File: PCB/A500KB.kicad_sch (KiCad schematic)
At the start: 251 parts, among them J1 Conn_01x31, J2 USB_B_Micro, J3 Conn_02x03_Odd_Even, J4 Conn_01x08_Male, J5 Conn_01x02, J6 Conn_01x04_Male, J7 Conn_01x04, Q1 MMBT3904, U1 IS32FL3237_DS, U2 AT90USB1287-A, Y2 16 MHz

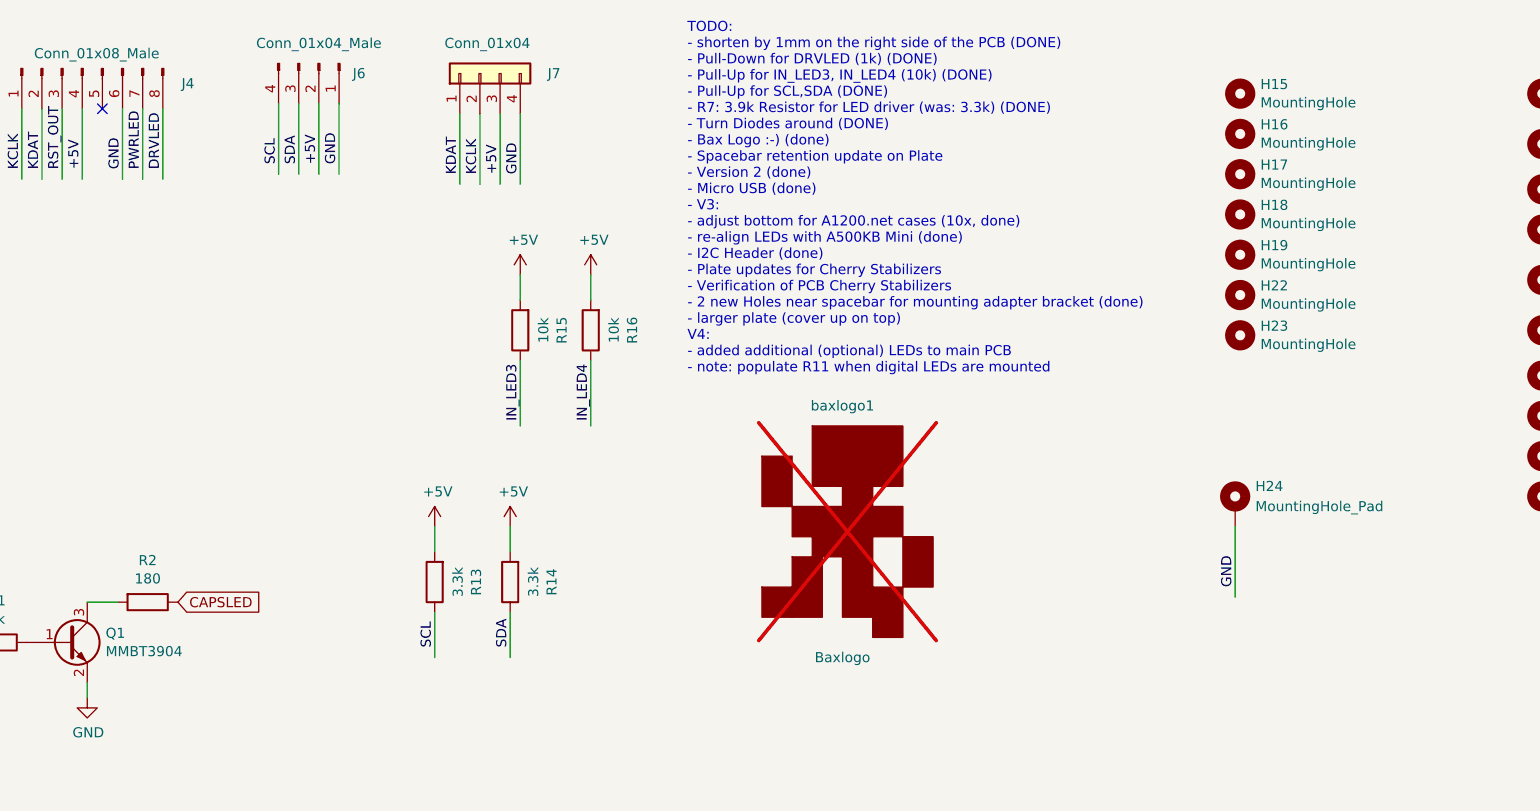
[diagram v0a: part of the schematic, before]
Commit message: V4c: fixed connector for A2k-A4k keyboard cables
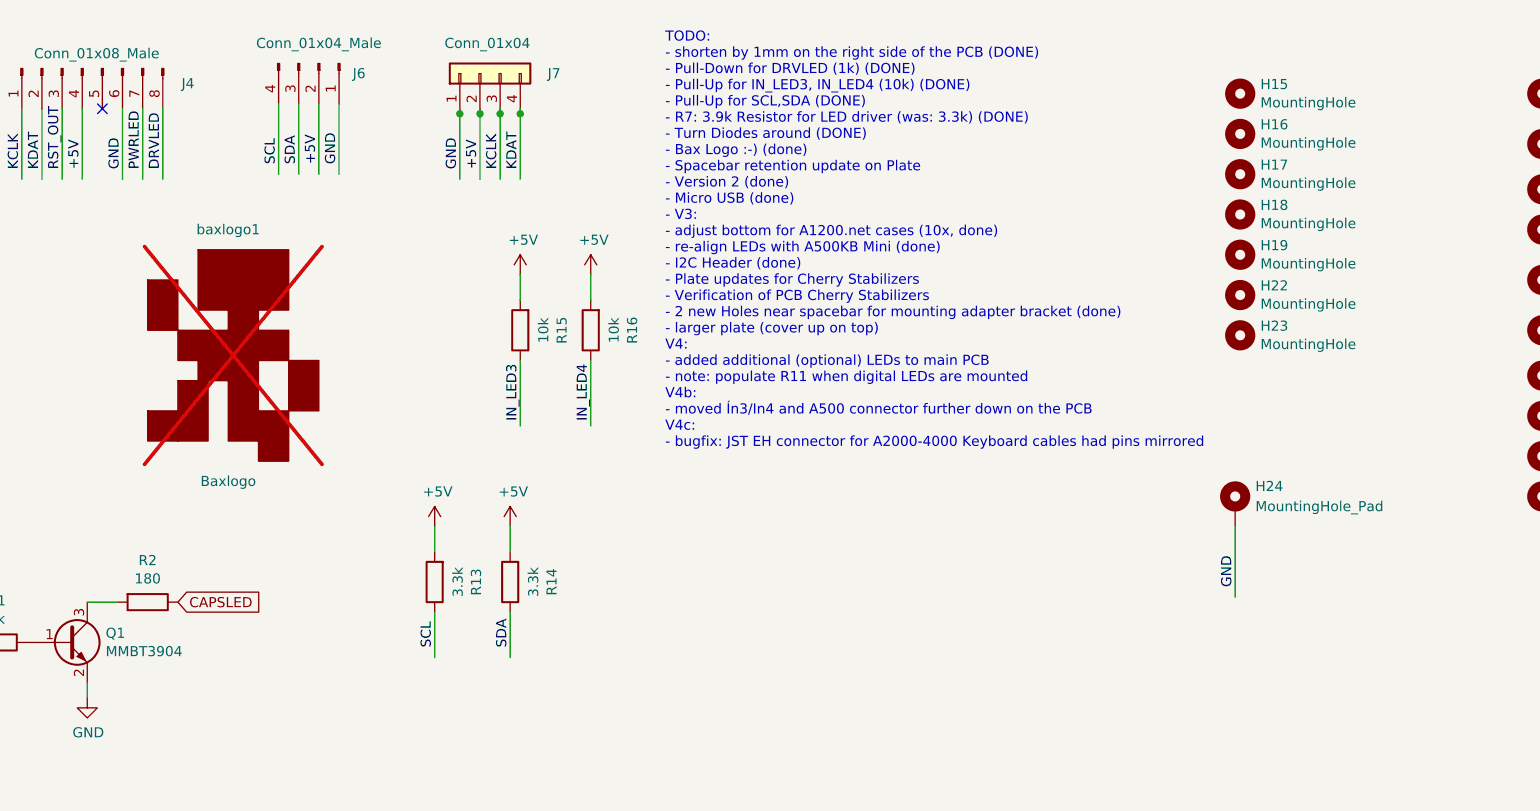
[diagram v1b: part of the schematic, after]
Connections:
- net +5V: now also J7.2 (Pin_2); no longer J7.3 (Pin_3)
- net GND: now also J7.1 (Pin_1); no longer J7.4 (Pin_4)
- net KCLK: now also J7.3 (Pin_3); no longer J7.2 (Pin_2)
- net KDAT: now also J7.4 (Pin_4); no longer J7.1 (Pin_1)
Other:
- moved on the sheet: baxlogo1
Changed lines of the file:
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@@
 	)
 	(junction
+		(at 252.73 26.035)
+		(diameter 0)
+		(color 0 0 0 0)
+	)
+	(junction
 		(at 132.08 354.33)
 		(diameter 0)
@@
 	)
 	(junction
+		(at 257.81 26.035)
+		(diameter 0)
+		(color 0 0 0 0)
+	)
+	(junction
 		(at 261.62 333.375)
 		(diameter 0)
@@
 	)
 	(junction
+		(at 250.19 26.035)
+		(diameter 0)
+		(color 0 0 0 0)
+	)
+	(junction
 		(at 257.175 234.315)
 		(diameter 0)
@@
 	)
 	(junction
+		(at 255.27 26.035)
+		(diameter 0)
+		(color 0 0 0 0)
+	)
+	(junction
 		(at 86.36 285.75)
 		(diameter 0)
@@
 	(wire
 		(pts
+			(xy 255.27 26.035) (xy 255.27 34.29)
+		)
+		(stroke
+			(width 0)
+			(type default)
+		)
+	)
+	(wire
+		(pts
 			(xy 71.12 376.555) (xy 86.36 376.555)
 		)
@@
 	(wire
 		(pts
-			(xy 257.81 26.035) (xy 257.81 34.925)
+			(xy 250.19 25.4) (xy 250.19 26.035)
 		)
 		(stroke
@@
 	(wire
 		(pts
+			(xy 257.81 26.035) (xy 257.81 34.29)
+		)
+		(stroke
+			(width 0)
+			(type default)
+		)
+	)
+	(wire
+		(pts
 			(xy 78.105 339.725) (xy 91.44 339.725)
 		)
@@
 	(wire
 		(pts
-			(xy 255.27 26.035) (xy 255.27 34.925)
+			(xy 252.73 25.4) (xy 252.73 26.035)
 		)
 		(stroke
@@
 	(wire
 		(pts
-			(xy 250.19 26.035) (xy 250.19 34.925)
+			(xy 257.81 25.4) (xy 257.81 26.035)
 		)
 		(stroke
@@
 	(wire
 		(pts
-			(xy 252.73 26.035) (xy 252.73 34.925)
+			(xy 255.27 25.4) (xy 255.27 26.035)
 		)
 		(stroke
@@
 	(wire
 		(pts
+			(xy 250.19 26.035) (xy 250.19 34.29)
+		)
+		(stroke
+			(width 0)
+			(type default)
+		)
+	)
+	(wire
+		(pts
 			(xy 170.815 297.18) (xy 170.815 300.99)
 		)
@@
 	(wire
 		(pts
+			(xy 252.73 26.035) (xy 252.73 34.29)
+		)
+		(stroke
+			(width 0)
+			(type default)
+		)
+	)
+	(wire
+		(pts
 			(xy 199.39 295.275) (xy 199.39 316.23)
 		)
@@
 		)
 	)
-	(text "TODO:\n- shorten by 1mm on the right side of the PCB (DONE)\n- Pull-Down for DRVLED (1k) (DONE)\n- Pull-Up for IN_LED3, IN_LED4 (10k) (DONE)\n- Pull-Up for SCL,SDA (DONE)\n- R7: 3.9k Resistor for LED driver (was: 3.3k) (DONE)\n- Turn Diodes around (DONE)\n- Bax Logo :-) (done)\n- Spacebar retention update on Plate\n- Version 2 (done)\n- Micro USB (done)\n- V3:\n- adjust bottom for A1200.net cases (10x, done)\n- re-align LEDs with A500KB Mini (done)\n- I2C Header (done)\n- Plate updates for Cherry Stabilizers\n- Verification of PCB Cherry Stabilizers\n- 2 new Holes near spacebar for mounting adapter bracket (done)\n- larger plate (cover up on top)\nV4:\n- added additional (optional) LEDs to main PCB\n- note: populate R11 when digital LEDs are mounted"
+	(text "TODO:\n- shorten by 1mm on the right side of the PCB (DONE)\n- Pull-Down for DRVLED (1k) (DONE)\n- Pull-Up for IN_LED3, IN_LED4 (10k) (DONE)\n- Pull-Up for SCL,SDA (DONE)\n- R7: 3.9k Resistor for LED driver (was: 3.3k) (DONE)\n- Turn Diodes around (DONE)\n- Bax Logo :-) (done)\n- Spacebar retention update on Plate\n- Version 2 (done)\n- Micro USB (done)\n- V3:\n- adjust bottom for A1200.net cases (10x, done)\n- re-align LEDs with A500KB Mini (done)\n- I2C Header (done)\n- Plate updates for Cherry Stabilizers\n- Verification of PCB Cherry Stabilizers\n- 2 new Holes near spacebar for mounting adapter bracket (done)\n- larger plate (cover up on top)\nV4:\n- added additional (optional) LEDs to main PCB\n- note: populate R11 when digital LEDs are mounted\nV4b:\n- moved Ín3/In4 and A500 connector further down on the PCB\nV4c:\n- bugfix: JST EH connector for A2000-4000 Keyboard cables had pins mirrored"
 		(exclude_from_sim no)
-		(at 278.892 58.928 0)
+		(at 276.098 68.326 0)
 		(effects
 			(font
@@
 	)
 	(label "KCLK"
-		(at 252.73 33.655 90)
+		(at 255.27 33.02 90)
 		(fields_autoplaced yes)
 		(effects
@@
 	)
 	(label "KDAT"
-		(at 250.19 33.655 90)
+		(at 257.81 33.02 90)
 		(fields_autoplaced yes)
 		(effects
@@
 	)
 	(label "+5V"
-		(at 255.27 33.655 90)
+		(at 252.73 33.02 90)
 		(fields_autoplaced yes)
 		(effects
@@
 	)
 	(label "GND"
-		(at 257.81 33.655 90)
+		(at 250.19 33.02 90)
 		(fields_autoplaced yes)
 		(effects
@@
 	(symbol
 		(lib_id "Graphic:Logo_Open_Hardware_Small")
-		(at 298.45 78.105 0)
+		(at 220.98 55.88 0)
 		(unit 1)
 		(exclude_from_sim no)
@@
 		(dnp yes)
 		(property "Reference" "baxlogo1"
-			(at 298.45 62.865 0)
+			(at 220.98 40.64 0)
 			(effects
 				(font
@@
 		)
 		(property "Value" "Baxlogo"
-			(at 298.45 94.615 0)
+			(at 220.98 72.39 0)
 			(effects
 				(font
@@
 		)
 		(property "Footprint" "Bax:baxlogo"
-			(at 299.72 76.835 0)
+			(at 222.25 54.61 0)
 			(effects
 				(font
@@
 		)
 		(property "Datasheet" "~"
-			(at 299.72 76.835 0)
+			(at 222.25 54.61 0)
 			(effects
 				(font
@@
 		)
 		(property "Description" ""
-			(at 298.45 78.105 0)
+			(at 220.98 55.88 0)
 			(effects
 				(font

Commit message: Hardware finetuning, Amiga program update
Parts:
- added R17: 150k, Resistor_SMD:R_0805_2012Metric_Pad1.20x1.40mm_HandSolder, symbol Device:R
- J1: value Conn_01x31 -> N/A
- J4: footprint Connector_PinHeader_2.54mm:PinHeader_1x08_P2.54mm_Vertical -> Connector_PinHeader_2.54mm:PinHeader_1x08_P2.54mm_Horizontal
- J5: footprint Connector_PinHeader_2.54mm:PinHeader_1x02_P2.54mm_Vertical -> Connector_PinHeader_2.54mm:PinHeader_1x02_P2.54mm_Horizontal; LCSC (none) -> C2935927
- J6: value Conn_01x04_Male -> N/A; DNP (none) -> true
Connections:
- net +5V: now also J7.3 (Pin_3); no longer J7.2 (Pin_2)
- net GND: now also J7.4 (Pin_4), R17.1; no longer J7.1 (Pin_1)
- net KCLK: now also J7.2 (Pin_2); no longer J7.3 (Pin_3)
- net KDAT: now also J7.1 (Pin_1); no longer J7.4 (Pin_4)
- net RST_OUT: now also R17.2
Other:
- note added: "TODO/Revision list: - shorten by 1mm on the right side of the PCB (DONE) - Pull-Down for DRVLED (1k) (DONE) - Pull-Up for IN_LED3, IN_LED4 (10k) (DONE) - Pull-Up for SCL,SDA (DONE) - R7: 3.9k Resistor for LED driver (was: 3.3k) (DONE) - Turn Diodes around (DONE) - Bax Logo :-) (done) - Spacebar retention update on Plate Version 2 (done) - Micro USB (done) V3: - adjust bottom for A1200.net cases (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"
- note removed: "TODO: - shorten by 1mm on the right side of the PCB (DONE) - Pull-Down for DRVLED (1k) (DONE) - Pull-Up for IN_LED3, IN_LED4 (10k) (DONE) - Pull-Up for SCL,SDA (DONE) - R7: 3.9k Resistor for LED driver (was: 3.3k) (DONE) - Turn Diodes around (DONE) - Bax Logo :-) (done) - Spacebar retention update on Plate - Version 2 (done) - Micro USB (done) - V3: - adjust bottom for A1200.net cases (10x, done)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"
- moved on the sheet: H24

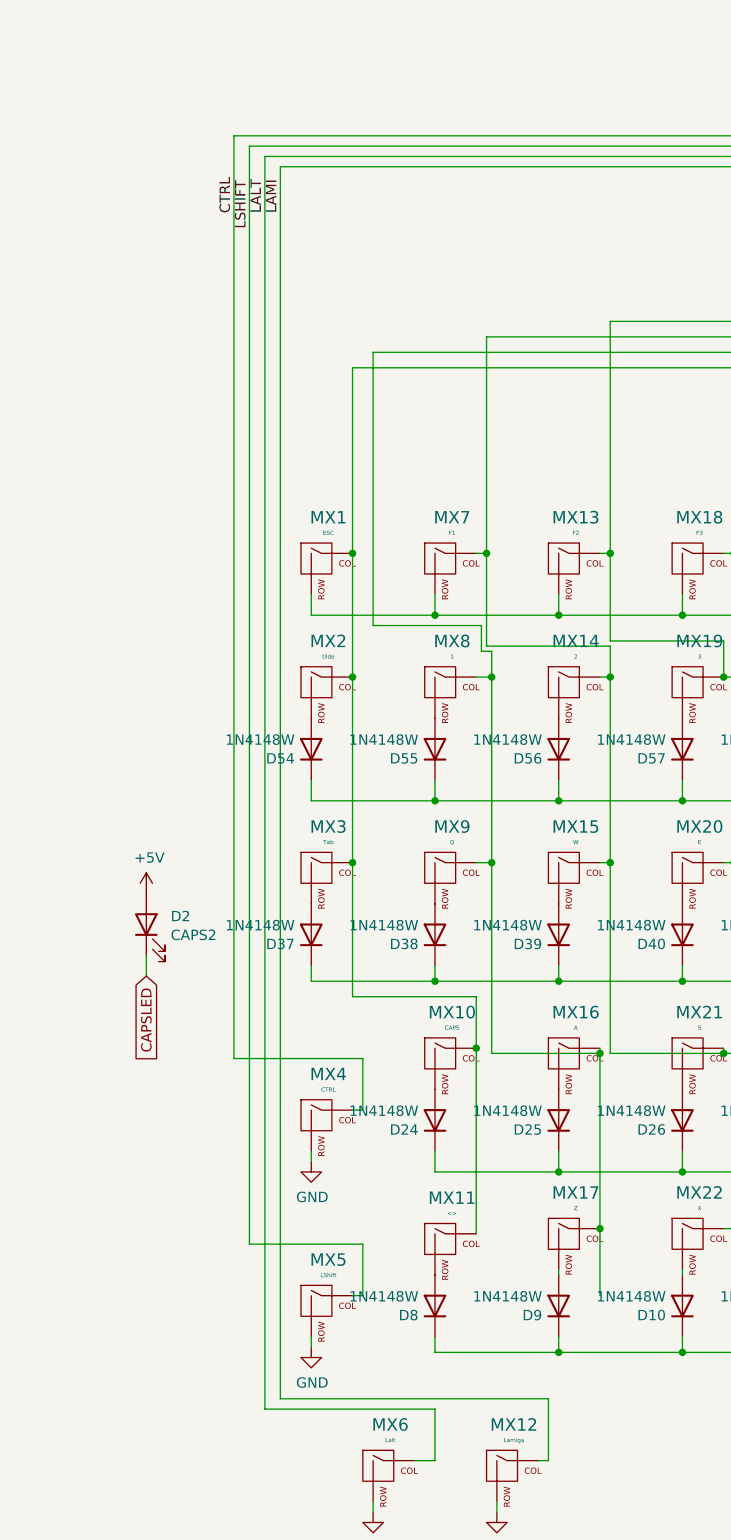
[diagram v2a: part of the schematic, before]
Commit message: unified 3D printed parts for internal/external use
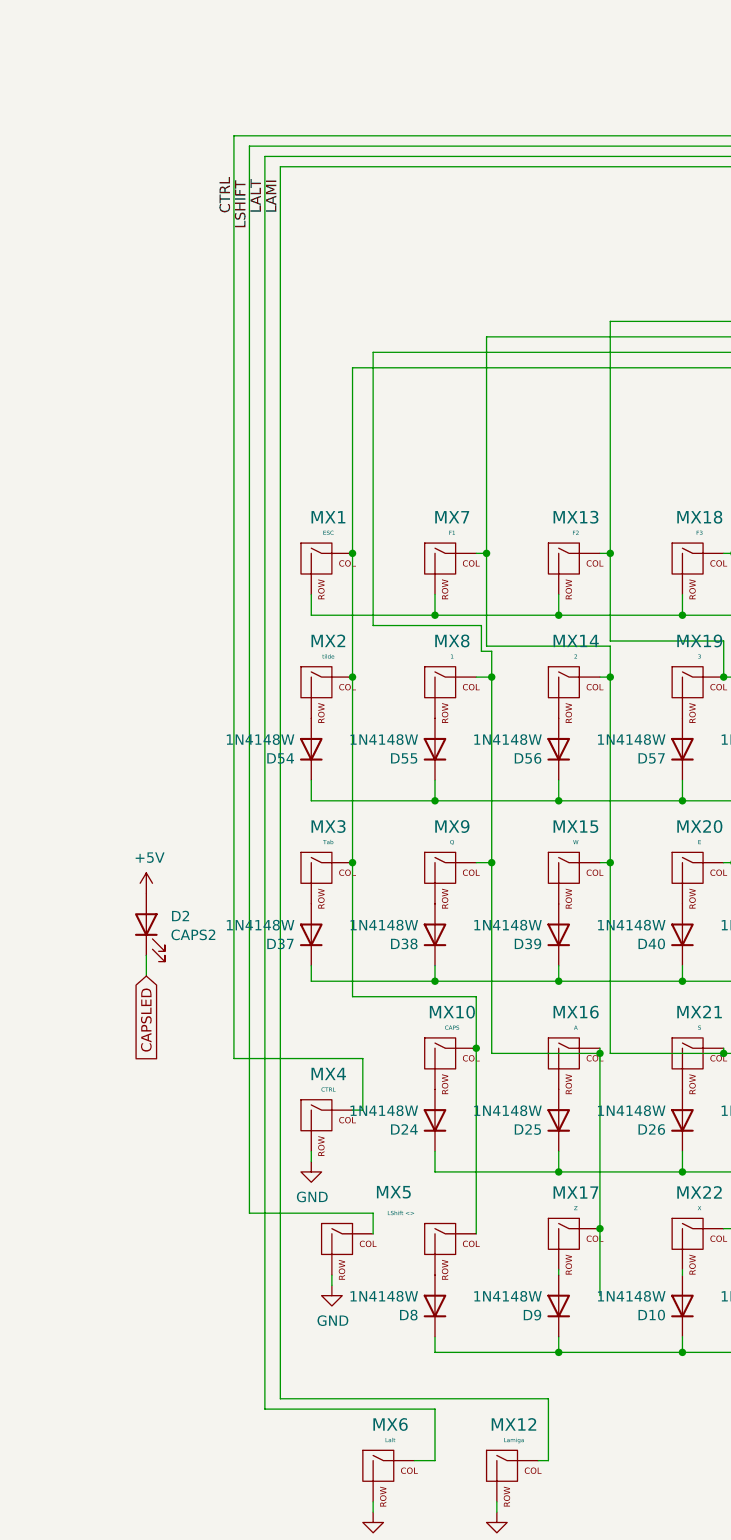
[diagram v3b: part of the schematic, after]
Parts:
- removed MX11: <>, MXMitsumi:MXMitsumi-1U-NoLED, symbol MX_Hybrid:MX-NoLED
- removed MX5: LShift, MXMitsumi:MXMitsumi-1.75U-NoLED, symbol MX_Hybrid:MX-NoLED
- added MX5: LShift <>, MXMitsumi:MXMitsumi-2.75U-SPCLEFT_LR, symbol MX_Hybrid:MX-LSHIFT_LR
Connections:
- net GND: now also MX5.2 (ROW)
- net LSHIFT: now also MX5.1 (COL)
- net Y14=15: now also MX5.3 (COL)
- net at D8.2 (A): now also MX5.4 (ROW)
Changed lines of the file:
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@@
 		(title "A500 Keyboard")
 		(date "2021-12-04")
-		(rev "0.0")
+		(rev "4e")
 		(company "Henryk Richter")
 	)
@@
 	(wire
 		(pts
+			(xy 63.5 361.95) (xy 63.5 359.41)
+		)
+		(stroke
+			(width 0)
+			(type default)
+		)
+	)
+	(wire
+		(pts
 			(xy 167.64 316.23) (xy 168.91 316.23)
 		)
@@
 	(wire
 		(pts
-			(xy 55.88 374.65) (xy 55.88 375.92)
+			(xy 58.42 367.03) (xy 58.42 368.3)
 		)
 		(stroke
@@
 	(wire
 		(pts
-			(xy 60.96 369.57) (xy 62.23 369.57)
-		)
-		(stroke
-			(width 0)
-			(type default)
-		)
-	)
-	(wire
-		(pts
 			(xy 387.35 344.17) (xy 386.08 344.17)
 		)
@@
 	(wire
 		(pts
+			(xy 48.26 359.41) (xy 48.26 227.965)
+		)
+		(stroke
+			(width 0)
+			(type default)
+		)
+	)
+	(wire
+		(pts
 			(xy 221.615 224.79) (xy 221.615 227.965)
 		)
@@
 	(wire
 		(pts
-			(xy 48.26 363.22) (xy 48.26 227.965)
-		)
-		(stroke
-			(width 0)
-			(type default)
-		)
-	)
-	(wire
-		(pts
 			(xy 515.62 86.995) (xy 526.415 86.995)
 		)
@@
 	(wire
 		(pts
-			(xy 62.23 369.57) (xy 62.23 363.22)
-		)
-		(stroke
-			(width 0)
-			(type default)
-		)
-	)
-	(wire
-		(pts
 			(xy 541.02 127) (xy 550.545 127)
 		)
@@
 	(wire
 		(pts
+			(xy 63.5 359.41) (xy 48.26 359.41)
+		)
+		(stroke
+			(width 0)
+			(type default)
+		)
+	)
+	(wire
+		(pts
 			(xy 249.555 240.03) (xy 391.16 240.03)
 		)
@@
 	(wire
 		(pts
-			(xy 62.23 363.22) (xy 48.26 363.22)
-		)
-		(stroke
-			(width 0)
-			(type default)
-		)
-	)
-	(wire
-		(pts
 			(xy 86.36 354.33) (xy 101.6 354.33)
 		)
@@
 	(symbol
 		(lib_id "MX_Hybrid:MX-NoLED")
-		(at 57.15 370.84 0)
-		(unit 1)
-		(exclude_from_sim no)
-		(in_bom yes)
-		(on_board yes)
-		(dnp no)
-		(property "Reference" "MX5"
-			(at 57.9882 365.1758 0)
-			(effects
-				(font
-					(size 1.524 1.524)
-				)
-			)
-		)
-		(property "Value" "LShift"
-			(at 57.9882 367.0554 0)
-			(effects
-				(font
-					(size 0.508 0.508)
-				)
-			)
-		)
-		(property "Footprint" "MXMitsumi:MXMitsumi-1.75U-NoLED"
-			(at 41.275 371.475 0)
-			(effects
-				(font
-					(size 1.524 1.524)
-				)
-				(hide yes)
-			)
-		)
-		(property "Datasheet" ""
-			(at 41.275 371.475 0)
-			(effects
-				(font
-					(size 1.524 1.524)
-				)
-				(hide yes)
-			)
-		)
-		(property "Description" ""
-			(at 57.15 370.84 0)
-			(effects
-				(font
-					(size 1.27 1.27)
-				)
-				(hide yes)
-			)
-		)
-		(pin "1"
-		)
-		(pin "2"
-		)
-		(instances
-			(project ""
-				(path "/0fb41543-9ec7-44b0-8d09-79a8fb596336"
-					(reference "MX5")
-					(unit 1)
-				)
-			)
-		)
-	)
-	(symbol
-		(lib_id "MX_Hybrid:MX-NoLED")
-		(at 72.39 363.22 0)
-		(unit 1)
-		(exclude_from_sim no)
-		(in_bom yes)
-		(on_board yes)
-		(dnp no)
-		(property "Reference" "MX11"
-			(at 73.2282 357.5558 0)
-			(effects
-				(font
-					(size 1.524 1.524)
-				)
-			)
-		)
-		(property "Value" "<>"
-			(at 73.2282 359.4354 0)
-			(effects
-				(font
-					(size 0.508 0.508)
-				)
-			)
-		)
-		(property "Footprint" "MXMitsumi:MXMitsumi-1U-NoLED"
-			(at 56.515 363.855 0)
-			(effects
-				(font
-					(size 1.524 1.524)
-				)
-				(hide yes)
-			)
-		)
-		(property "Datasheet" ""
-			(at 56.515 363.855 0)
-			(effects
-				(font
-					(size 1.524 1.524)
-				)
-				(hide yes)
-			)
-		)
-		(property "Description" ""
-			(at 72.39 363.22 0)
-			(effects
-				(font
-					(size 1.27 1.27)
-				)
-				(hide yes)
-			)
-		)
-		(pin "1"
-		)
-		(pin "2"
-		)
-		(instances
-			(project ""
-				(path "/0fb41543-9ec7-44b0-8d09-79a8fb596336"
-					(reference "MX11")
-					(unit 1)
-				)
-			)
-		)
-	)
-	(symbol
-		(lib_id "MX_Hybrid:MX-NoLED")
 		(at 87.63 362.585 0)
 		(unit 1)
@@
 	(symbol
 		(lib_id "power:GND")
-		(at 55.88 375.92 0)
+		(at 58.42 368.3 0)
 		(unit 1)
 		(exclude_from_sim no)
@@
 		(dnp no)
 		(property "Reference" "#PWR0105"
-			(at 55.88 382.27 0)
+			(at 58.42 374.65 0)
 			(effects
 				(font
@@
 		)
 		(property "Value" "GND"
-			(at 56.007 380.3142 0)
+			(at 58.547 372.6942 0)
 			(effects
 				(font
@@
 		)
 		(property "Footprint" ""
-			(at 55.88 375.92 0)
+			(at 58.42 368.3 0)
 			(effects
 				(font
@@
 		)
 		(property "Datasheet" ""
-			(at 55.88 375.92 0)
+			(at 58.42 368.3 0)
 			(effects
 				(font
@@
 		)
 		(property "Description" ""
-			(at 55.88 375.92 0)
+			(at 58.42 368.3 0)
 			(effects
 				(font
@@
 					(unit 1)
 				)
+			)
+		)
+	)
+	(symbol
+		(lib_id "MX_Hybrid:MX-LSHIFT_LR")
+		(at 59.69 363.22 0)
+		(unit 1)
+		(exclude_from_sim no)
+		(in_bom yes)
+		(on_board yes)
+		(dnp no)
+		(property "Reference" "MX5"
+			(at 66.04 356.87 0)
+			(effects
+				(font
+					(size 1.524 1.524)
+				)
+			)
+		)
+		(property "Value" "LShift <>"
+			(at 66.9352 359.41 0)
+			(effects
+				(font
+					(size 0.508 0.508)
+				)
+			)
+		)
+		(property "Footprint" "MXMitsumi:MXMitsumi-2.75U-SPCLEFT_LR"
+			(at 43.815 363.855 0)
+			(effects
+				(font
+					(size 1.524 1.524)
+				)
+				(hide yes)
+			)
+		)
+		(property "Datasheet" ""
+			(at 43.815 363.855 0)
+			(effects
+				(font
+					(size 1.524 1.524)
+				)
+				(hide yes)
+			)
+		)
+		(property "Description" ""
+			(at 59.69 363.22 0)
+			(effects
+				(font
+					(size 1.27 1.27)
+				)
+				(hide yes)
+			)
+		)
+		(pin "4"
+		)
+		(pin "3"
+		)
+		(pin "2"
+		)
+		(pin "1"
+		)
+		(instances
+			(project ""
+				(path "/0fb41543-9ec7-44b0-8d09-79a8fb596336"
+					(reference "MX5")
+					(unit 1)
+				)
